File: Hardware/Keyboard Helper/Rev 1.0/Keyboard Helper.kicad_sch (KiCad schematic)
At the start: 91 parts, among them J1 PORT A, J2 PORT B, J3 KEYBOARD, J4 JOYSTICK A, J5 JOYSTICK B, J6 JOYSTICK A, J7 JOYSTICK B, SW1 DEL, SW10 R, SW11 D, SW12 6, SW13 7, SW14 Y, SW15 G, SW16 8, SW17 9, SW18 I, SW19 J, SW2 RETURN, SW20 0, SW21 +, SW22 P, SW23 L, SW24 -, SW25 £, SW26 *, SW27 ;, SW28 HOME, SW29 1, SW3 LEFT/RIGHT, SW30 LEFT ARROW, SW31 CTRL, SW32 2, SW33 F1, SW34 F3, SW35 F5, SW36 UP/DOWN, SW37 Z, SW38 S, SW39 E, SW4 F7, SW40 L SHIFT, SW41 C, SW42 F, SW43 T, SW44 X, SW45 B, SW46 H, SW47 U, SW48 V, SW49 M, SW5 3, SW50 K, SW51 O, SW52 N, SW53 ., SW54 :, SW55 @, SW56 ,, SW57 R SHIFT, SW58 =, SW59 UP ARROW, SW6 W, SW60 /, SW61 SPACE, SW62 C64, SW63 Q, SW64 RUN/STOP, SW7 A, SW8 4, SW9 5

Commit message: Fix for Keypad LCD Helper silkscreen
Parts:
- J3: Digikey (none) -> 19-88625-5005-ND
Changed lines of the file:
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@@
+			)
+		)
+		(property "Digikey" "19-88625-5005-ND"
+			(at 121.92 185.42 90)
+			(effects
+				(font
+					(size 1.27 1.27)
+				)
+				(hide yes)
 			)
 		)

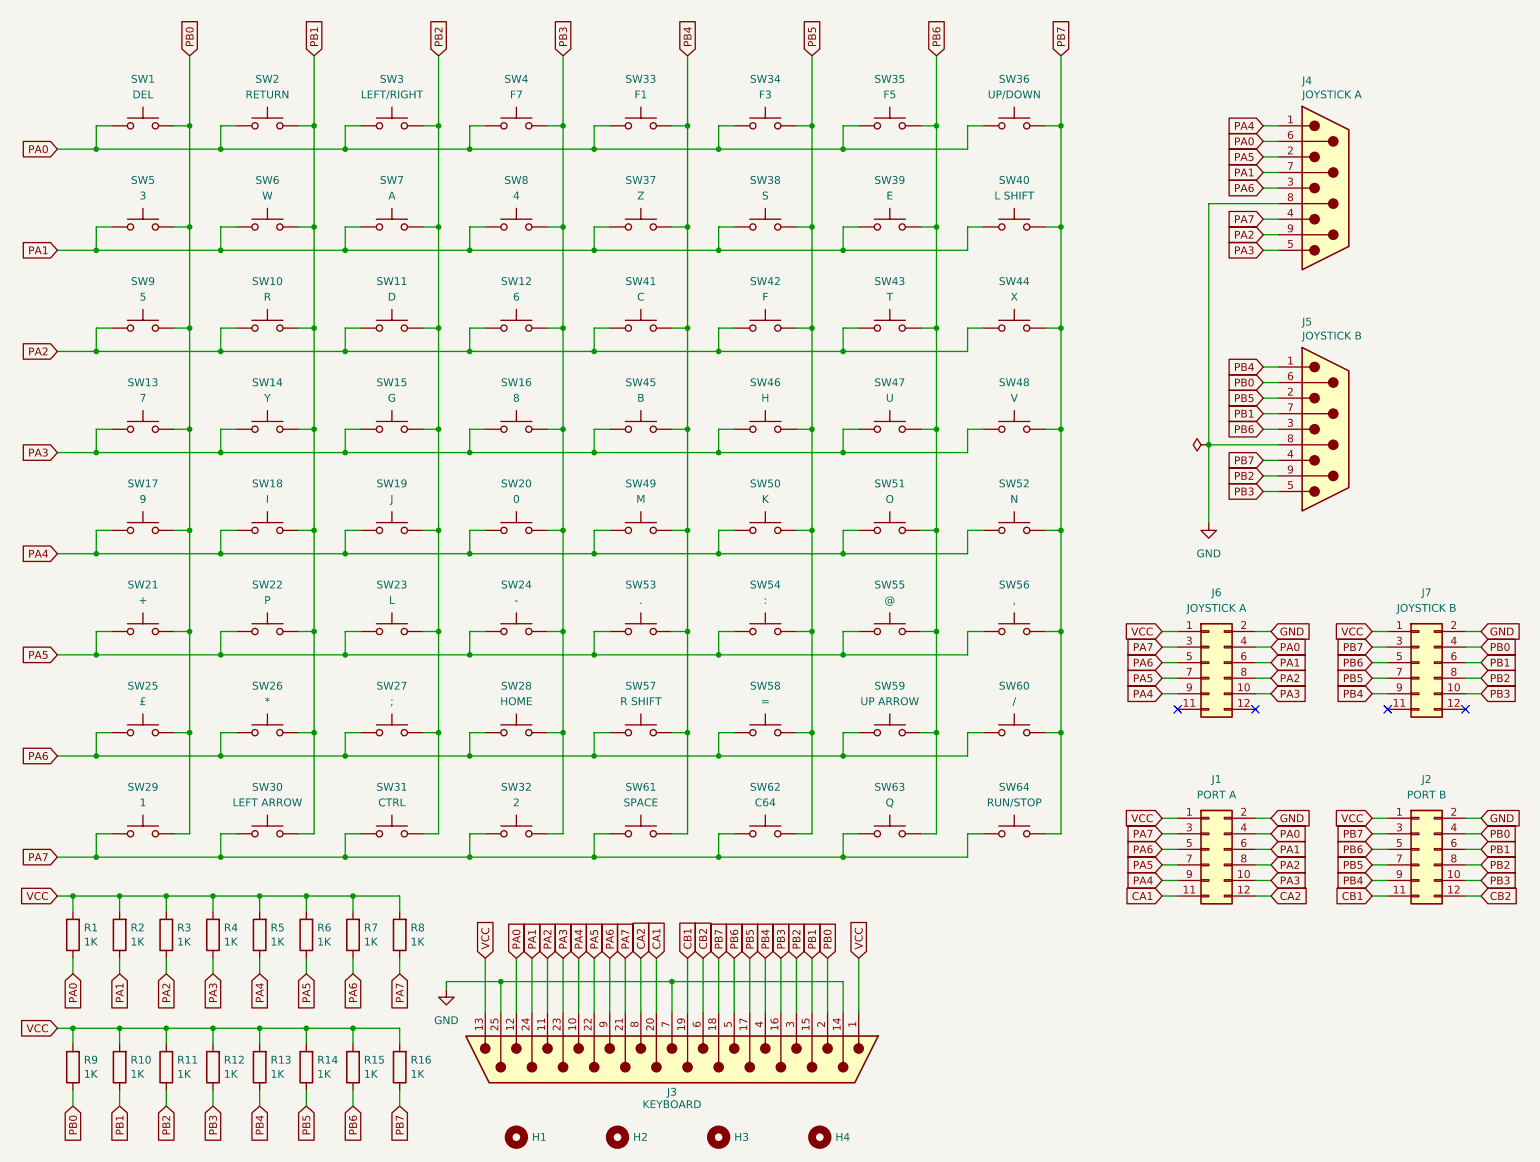
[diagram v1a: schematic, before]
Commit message: Fix DB Connectors
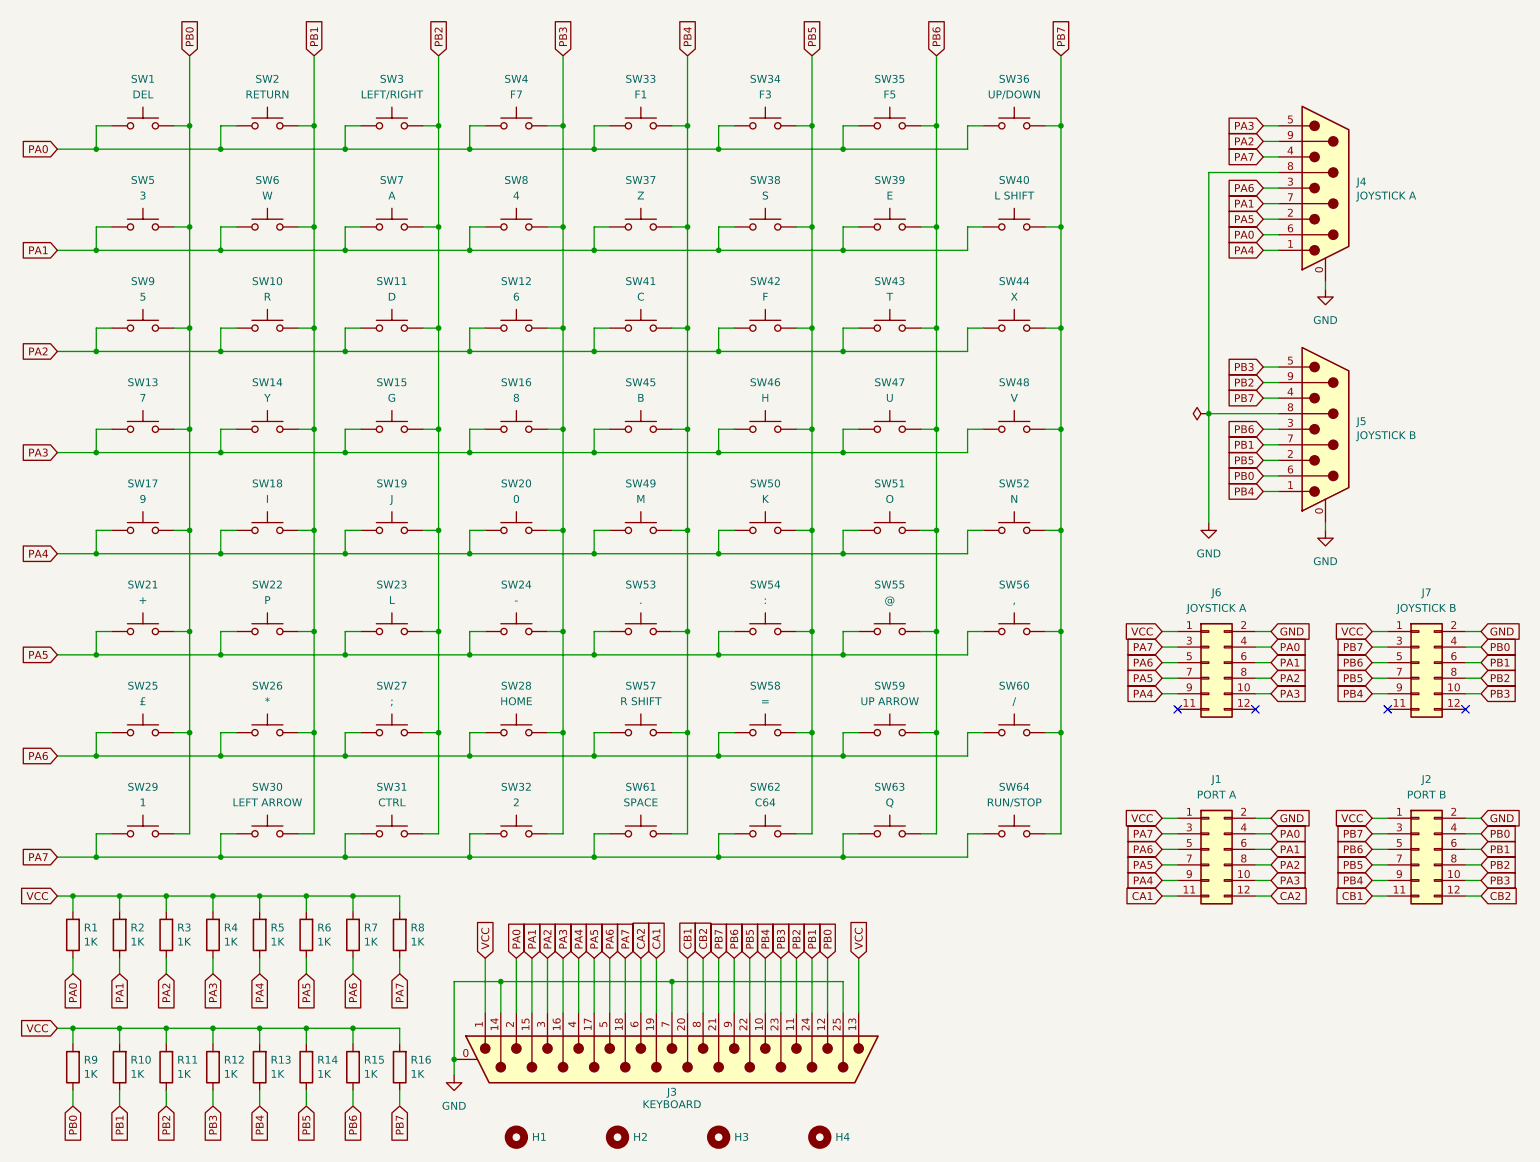
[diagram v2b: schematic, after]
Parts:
- J3: footprint (none) -> Connector_Dsub:DSUB-25_Pins_Horizontal_P2.77x2.84mm_EdgePinOffset7.70mm_Housed_MountingHolesOffset9.12mm; symbol Connector:DB25_Pins -> Connector:DB25_Pins_MountingHoles
- J4, J5: footprint 6502 Parts:DB9 Male -> Connector_Dsub:DSUB-9_Pins_Horizontal_P2.77x2.84mm_EdgePinOffset7.70mm_Housed_MountingHolesOffset9.12mm; symbol 6502 Parts:DB9 Male -> Connector:DE9_Pins_MountingHoles; now in the parts list
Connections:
- net CA1: now also J3.19 (P19); no longer J3.20 (P20)
- net CA2: now also J3.6; no longer J3.8
- net CB1: now also J3.20 (P20); no longer J3.19 (P19)
- net CB2: now also J3.8; no longer J3.6
- net GND: now also J3.0 (PAD), J4.0 (PAD), J5.0 (PAD)
- net PA0: now also J3.2; no longer J3.12
- net PA1: now also J3.15 (P15); no longer J3.24 (P24)
- net PA2: now also J3.3; no longer J3.11
- net PA3: now also J3.16 (P16); no longer J3.23 (P23)
- net PA4: now also J3.4; no longer J3.10
- net PA5: now also J3.17 (P17); no longer J3.22 (P22)
- net PA6: now also J3.5; no longer J3.9
- net PA7: now also J3.18 (P18); no longer J3.21 (P21)
- net PB0: now also J3.12; no longer J3.2
- net PB1: now also J3.24 (P24); no longer J3.15 (P15)
- net PB2: now also J3.11; no longer J3.3
- net PB3: now also J3.23 (P23); no longer J3.16 (P16)
- net PB4: now also J3.10; no longer J3.4
- net PB5: now also J3.22 (P22); no longer J3.17 (P17)
- net PB6: now also J3.9; no longer J3.5
- net PB7: now also J3.21 (P21); no longer J3.18 (P18)

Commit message: More parts cleanup
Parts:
- J3: Digikey 19-88625-5005-ND -> 609-1505-ND; MPN (none) -> D25P33E4GX00LF
- J4, J5: Digikey (none) -> 609-1481-ND; MPN (none) -> D09P33E4GX00LF; Sparkfun PRT-00429 -> (none)
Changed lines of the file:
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@@
 			)
 		)
-		(property "Sparkfun" "PRT-00429"
+		(property "Digikey" "609-1481-ND"
+			(at 228.6 43.18 0)
+			(effects
+				(font
+					(size 1.27 1.27)
+				)
+				(hide yes)
+			)
+		)
+		(property "MPN" "D09P33E4GX00LF"
 			(at 228.6 43.18 0)
 			(effects
@@
 			)
 		)
-		(property "Digikey" "19-88625-5005-ND"
+		(property "Digikey" "609-1505-ND"
+			(at 121.92 185.42 90)
+			(effects
+				(font
+					(size 1.27 1.27)
+				)
+				(hide yes)
+			)
+		)
+		(property "MPN" "D25P33E4GX00LF"
 			(at 121.92 185.42 90)
 			(effects
@@
 			)
 		)
-		(property "Sparkfun" "PRT-00429"
+		(property "Digikey" "609-1481-ND"
 			(at 228.6 82.55 0)
 			(effects
+				(font
+					(size 1.27 1.27)
+				)
+				(hide yes)
+			)
+		)
+		(property "MPN" "D09P33E4GX00LF"
+			(at 228.6 82.55 0)
+			(effects

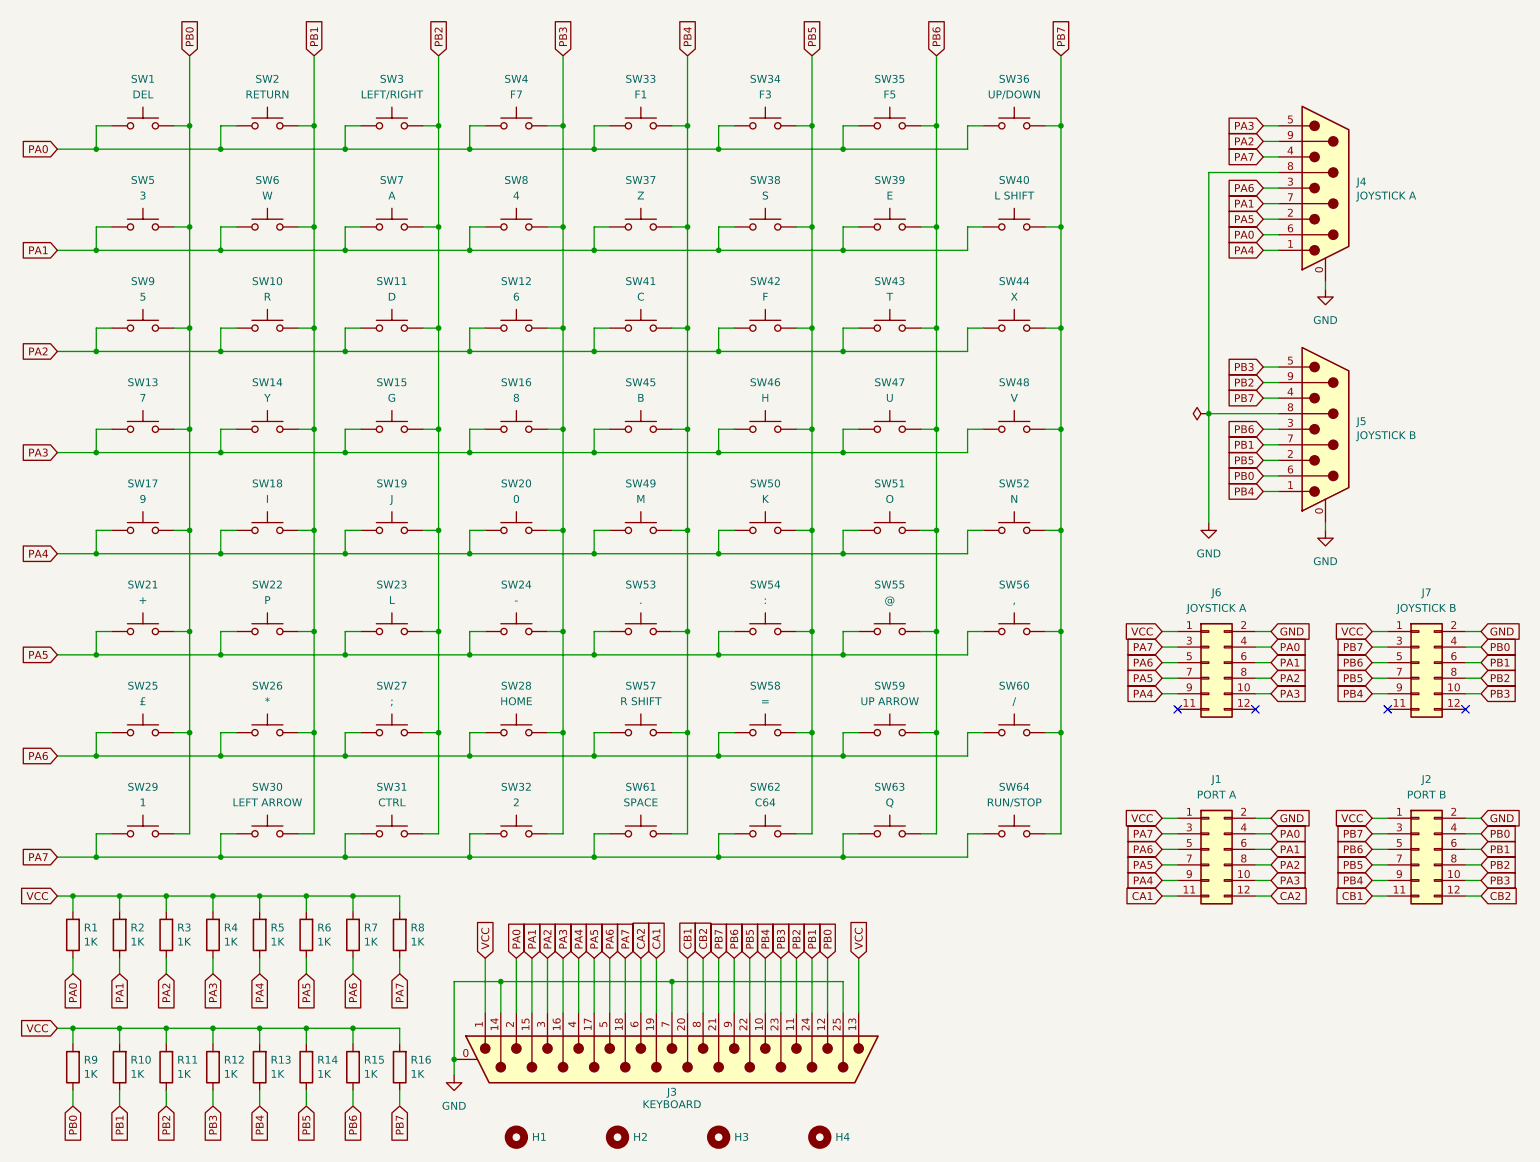
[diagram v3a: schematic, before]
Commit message: Add GPIO DB25 Helper
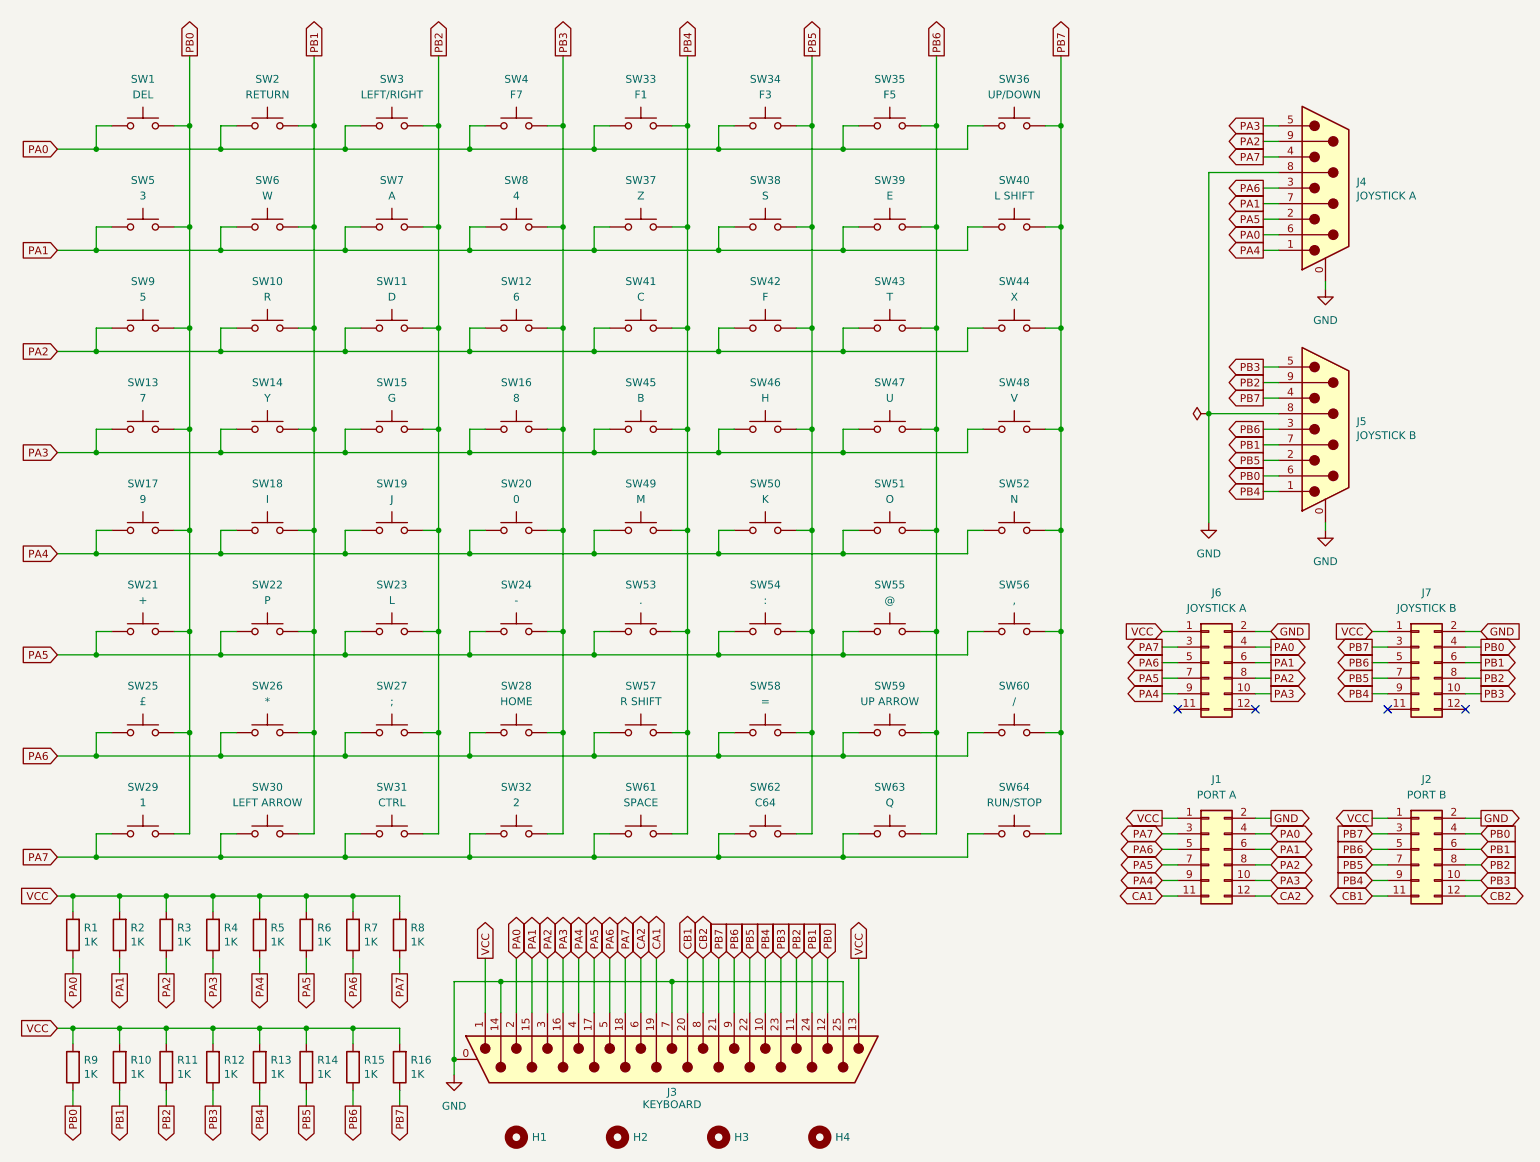
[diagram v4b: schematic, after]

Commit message: Housekeeping
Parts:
- removed H1, H2, H3, H4: MountingHole, MountingHole:MountingHole_3.2mm_M3, symbol Mechanical:MountingHole
